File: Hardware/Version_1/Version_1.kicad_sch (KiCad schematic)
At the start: 90 parts, among them IC1 W25R256JVEIQ, IC3 TPS62A01DRLR, IC4 TPS62A01DRLR, IC5 TPS62A01DRLR, IC6 LIFCL-40-7BG256C, IC7 IS46TR16128D-125KBLA2, J1 GPIO, J2 52435-2271, J3 Conn_01x05_Pin, J4 52435-2271, U1 CAT24C256

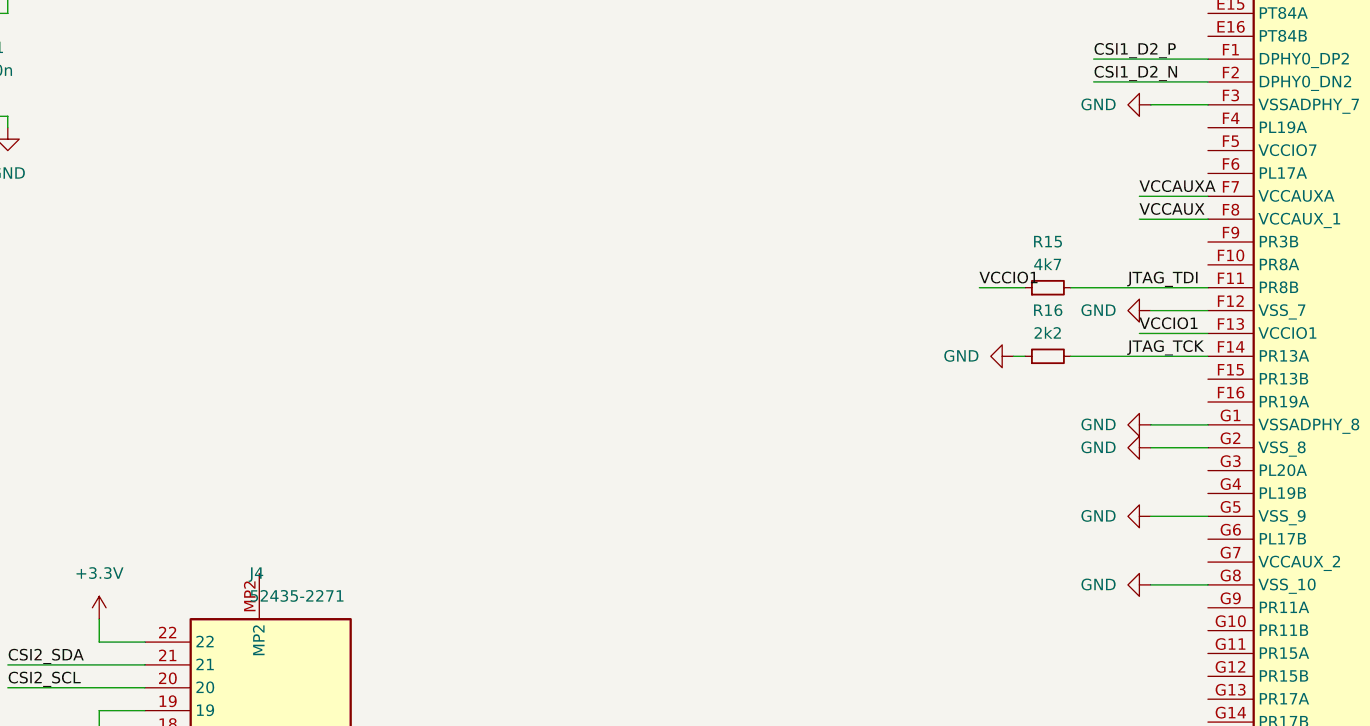
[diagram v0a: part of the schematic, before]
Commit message: added pll
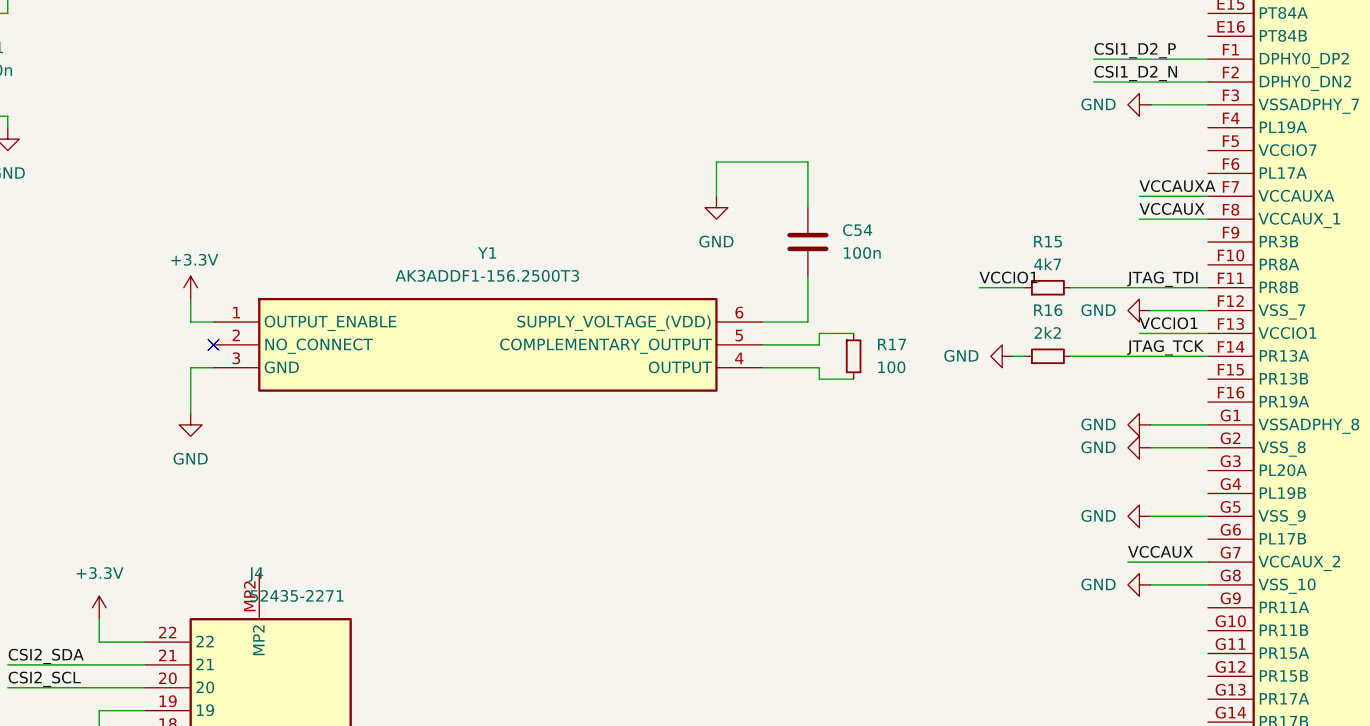
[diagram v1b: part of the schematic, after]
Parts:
- added C54: 100n, Capacitor_SMD:C_0603_1608Metric, symbol Device:C
- added R17: 100, Resistor_SMD:R_0603_1608Metric, symbol Device:R_Small
- added Y1: AK3ADDF1-156.2500T3, Component:AK3ADDF11562500T3, symbol Component:AK3ADDF1-156.2500T3
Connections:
- net +3V3: now also Y1.1 (OUTPUT_ENABLE)
- net GND: now also C54.1, Y1.3 (GND)
- net VCCAUX: now also IC6.G7 (VCCAUX_2)
- new net: C54.2, Y1.6 (SUPPLY_VOLTAGE_(VDD))
- new net: R17.1, Y1.5 (COMPLEMENTARY_OUTPUT)
- new net: R17.2, Y1.4 (OUTPUT)
- no-connect marks 20 -> 21

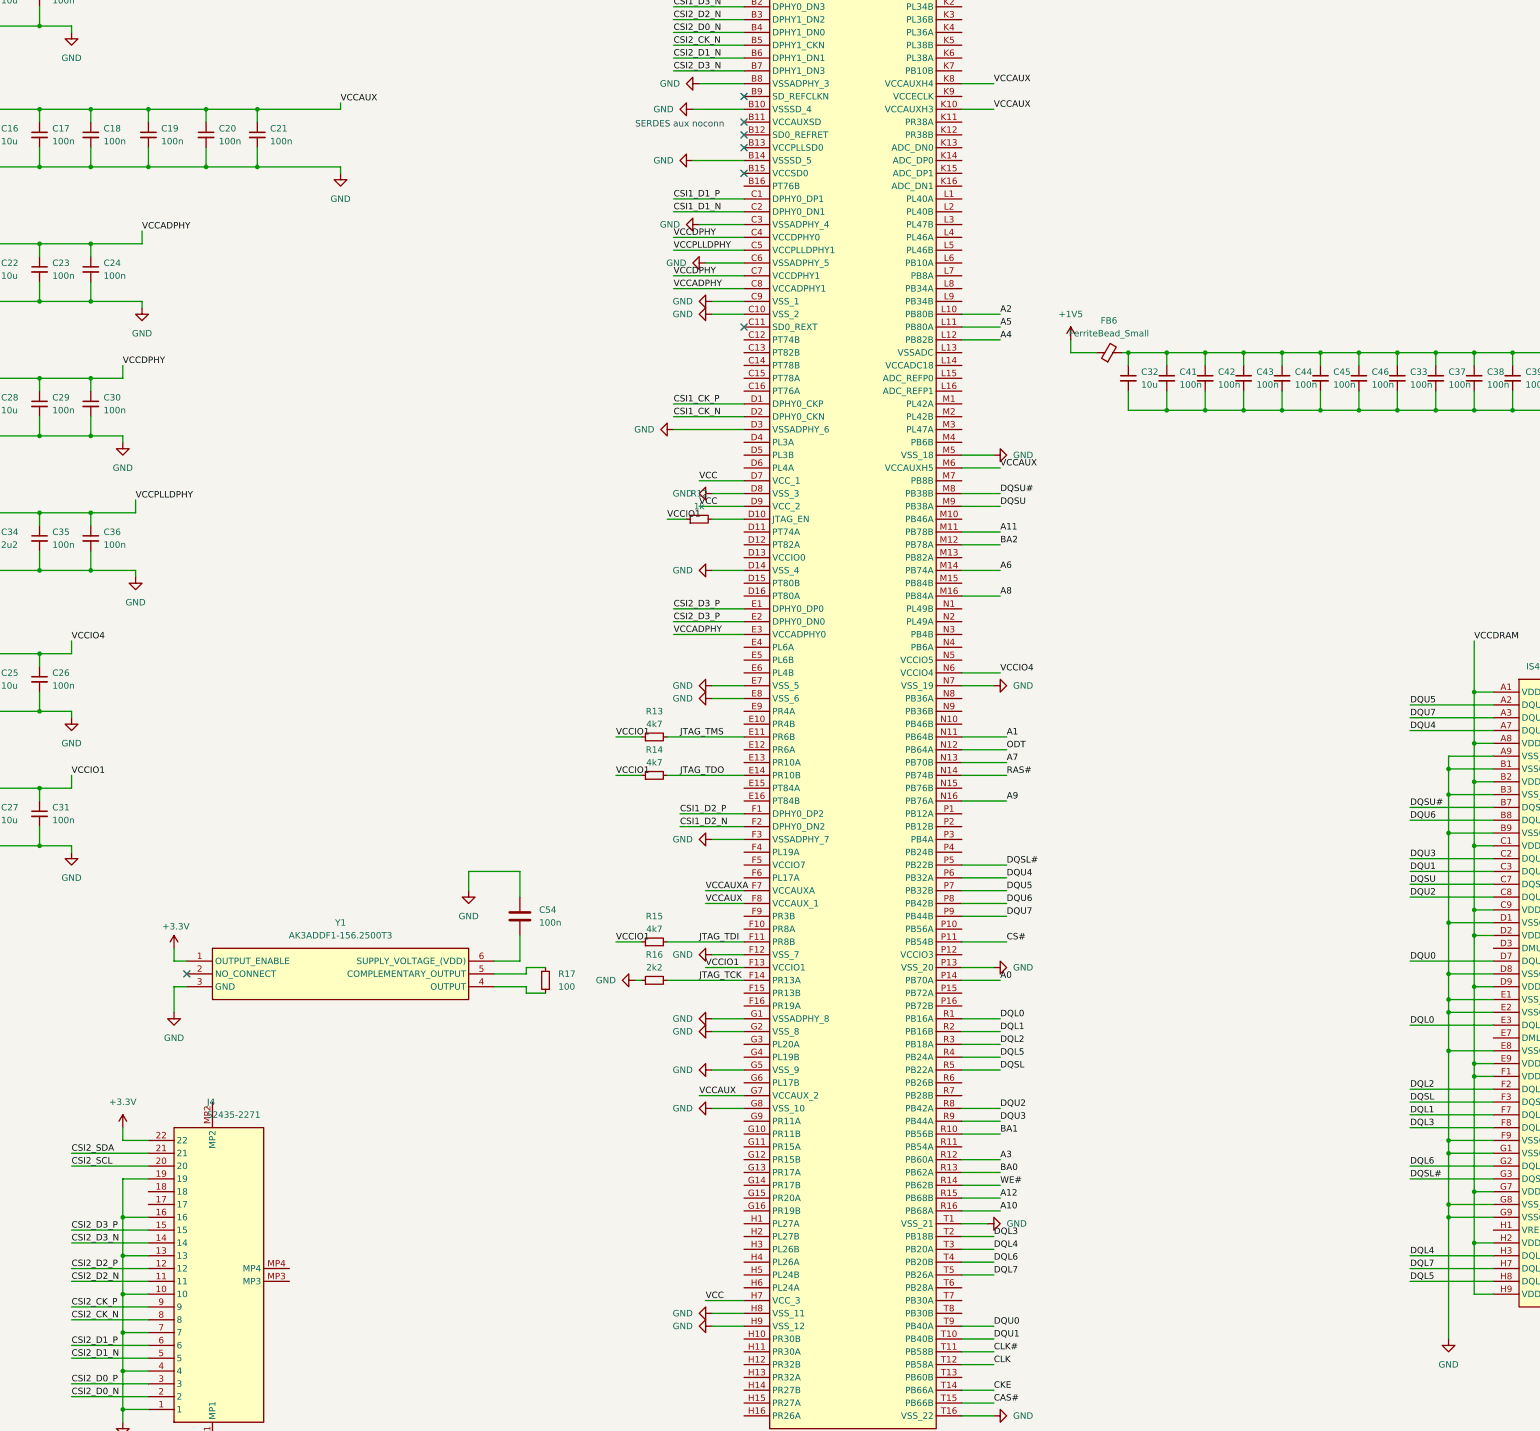
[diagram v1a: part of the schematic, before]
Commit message: Done routing for first DQS group
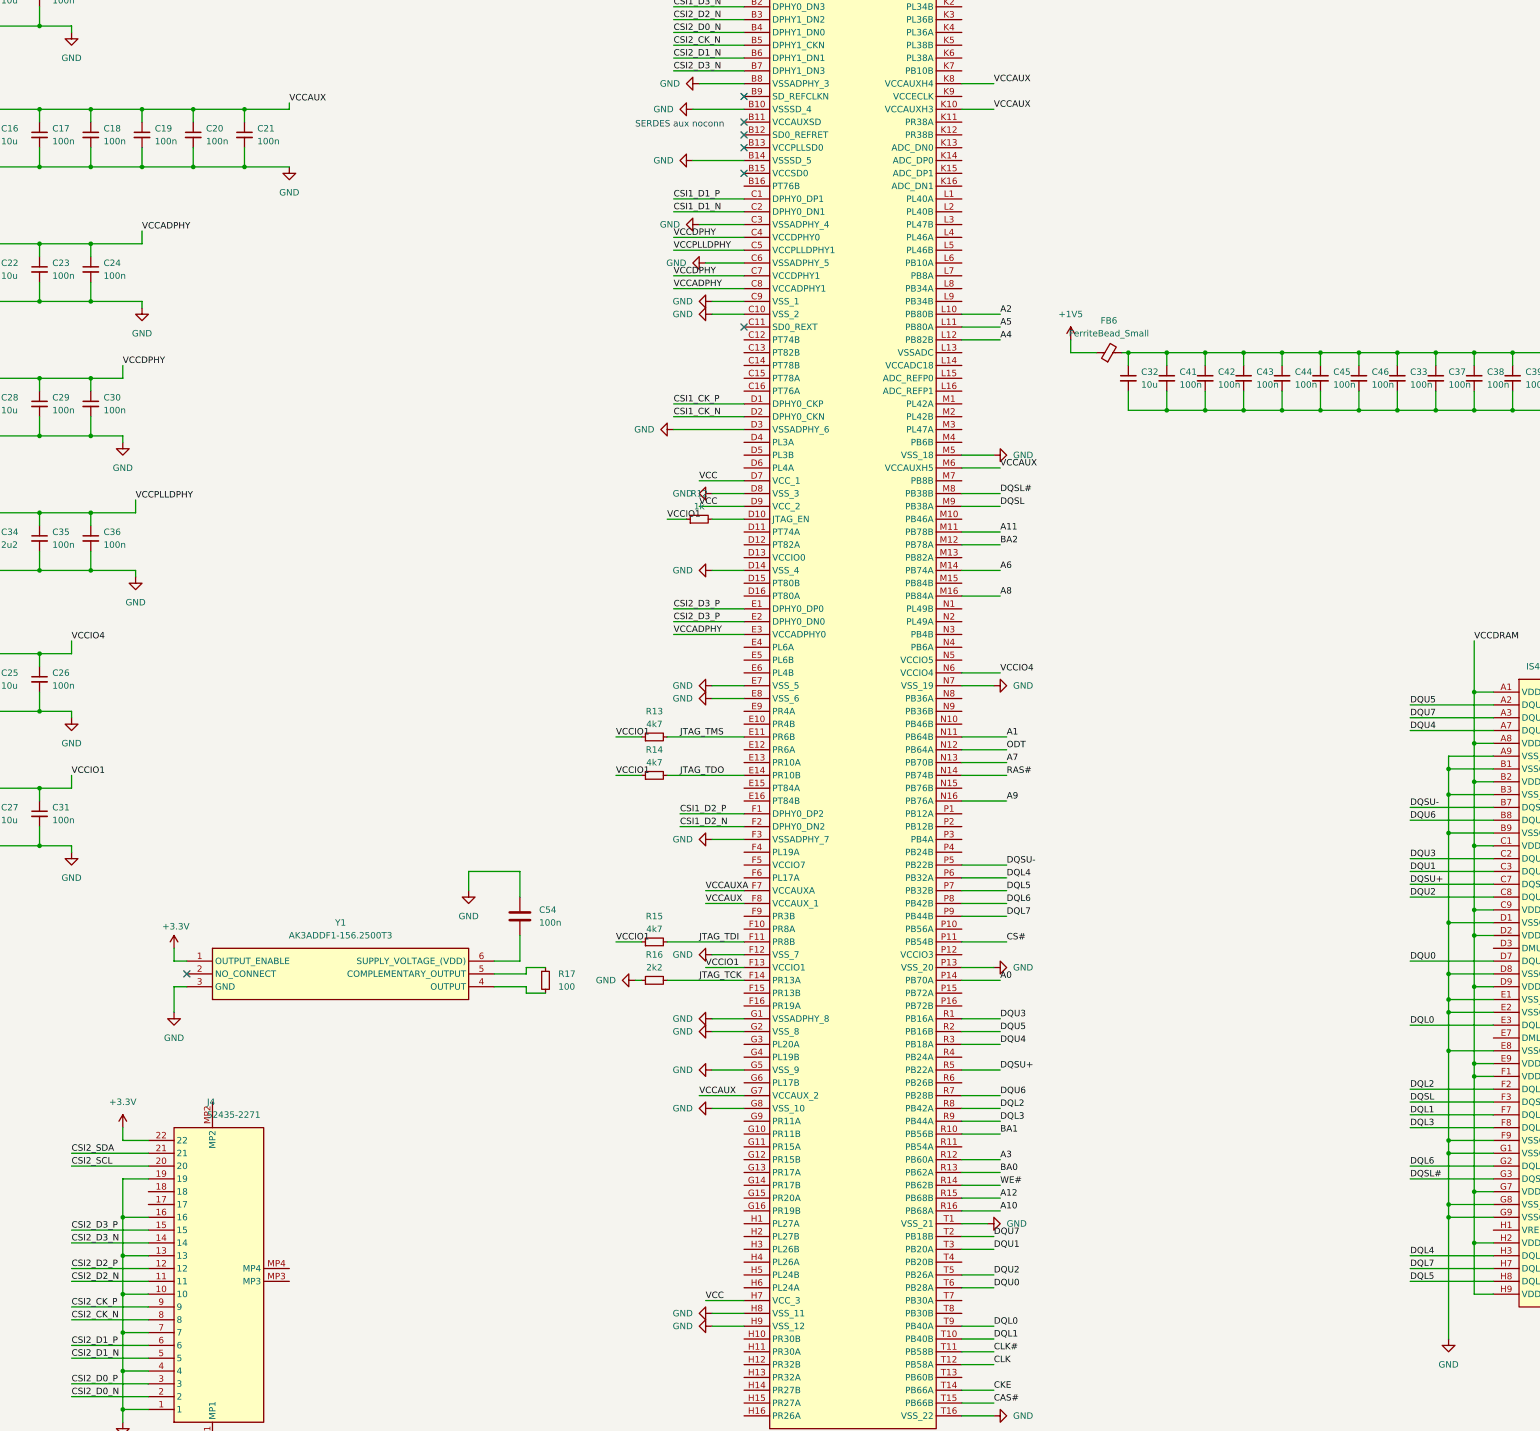
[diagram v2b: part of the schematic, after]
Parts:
- C14, C22, C25, C27, C28, C32, C34, C54, C9: footprint Capacitor_SMD:C_0603_1608Metric -> Capacitor_SMD:C_0402_1005Metric
- R13, R14, R15, R16: footprint Resistor_SMD:R_0603_1608Metric -> Resistor_SMD:R_0402_1005Metric
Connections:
- net DQL0: now also IC6.T9 (PB40A); no longer IC6.R1 (PB16A)
- net DQL1: now also IC6.T10 (PB40B); no longer IC6.R2 (PB16B)
- net DQL2: now also IC6.R8 (PB42A); no longer IC6.R3 (PB18A)
- net DQL3: now also IC6.R9 (PB44A); no longer IC6.T2 (PB18B)
- net DQL4: now also IC6.P6 (PB32A); no longer IC6.T3 (PB20A)
- net DQL5: now also IC6.P7 (PB32B); no longer IC6.R4 (PB24A)
- net DQL6: now also IC6.P8 (PB42B); no longer IC6.T4 (PB20B)
- net DQL7: now also IC6.P9 (PB44B); no longer IC6.T5 (PB26A)
- net DQSL: now also IC6.M9 (PB38A); no longer IC6.R5 (PB22A)
- net DQSL#: now also IC6.M8 (PB38B); no longer IC6.P5 (PB22B)
- net DQU0: now also IC6.T6 (PB28A); no longer IC6.T9 (PB40A)
- net DQU1: now also IC6.T3 (PB20A); no longer IC6.T10 (PB40B)
- net DQU2: now also IC6.T5 (PB26A); no longer IC6.R8 (PB42A)
- net DQU3: now also IC6.R1 (PB16A); no longer IC6.R9 (PB44A)
- net DQU4: now also IC6.R3 (PB18A); no longer IC6.P6 (PB32A)
- net DQU5: now also IC6.R2 (PB16B); no longer IC6.P7 (PB32B)
- net DQU6: now also IC6.R7 (PB28B); no longer IC6.P8 (PB42B)
- net DQU7: now also IC6.T2 (PB18B); no longer IC6.P9 (PB44B)
- net DQSU renamed DQSU+
- net DQSU+: now also IC6.R5 (PB22A); no longer IC6.M9 (PB38A)
- net DQSU# renamed DQSU-
- net DQSU-: now also IC6.P5 (PB22B); no longer IC6.M8 (PB38B)
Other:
- moved on the sheet: C19, C20, C21

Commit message: DRAM DQ groups
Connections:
- net DQL1: now also IC6.P6 (PB32A)
- net DQL3: now also IC6.P7 (PB32B)
- net DQL4: no longer IC6.P6 (PB32A)
- net DQL5: no longer IC6.P7 (PB32B)
- net DQSL renamed DQSL_P
- net DQSL# renamed DQSL_N
- net DQSU+ renamed DQSU_P
- net DQSU- renamed DQSU_N
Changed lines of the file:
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@@
     (effects (font (size 1.27 1.27)) (justify left bottom))
   )
-  (label "DQSU-" (at 487.68 252.73 0) (fields_autoplaced)
+  (label "DQSU_N" (at 487.68 252.73 0) (fields_autoplaced)
     (effects (font (size 1.27 1.27)) (justify left bottom))
   )
@@
     (effects (font (size 1.27 1.27)) (justify left bottom))
   )
-  (label "DQSU+" (at 487.68 267.97 0) (fields_autoplaced)
+  (label "DQSU_P" (at 487.68 267.97 0) (fields_autoplaced)
     (effects (font (size 1.27 1.27)) (justify left bottom))
   )
@@
     (effects (font (size 1.27 1.27)) (justify left bottom))
   )
-  (label "DQSL" (at 487.68 311.15 0) (fields_autoplaced)
+  (label "DQSL_P" (at 487.68 311.15 0) (fields_autoplaced)
     (effects (font (size 1.27 1.27)) (justify left bottom))
   )
@@
     (effects (font (size 1.27 1.27)) (justify left bottom))
   )
-  (label "DQSU-" (at 407.67 264.16 0) (fields_autoplaced)
+  (label "DQSU_N" (at 407.67 264.16 0) (fields_autoplaced)
     (effects (font (size 1.27 1.27)) (justify left bottom))
   )
@@
     (effects (font (size 1.27 1.27)) (justify right bottom))
   )
-  (label "DQSL" (at 406.4 193.04 0) (fields_autoplaced)
+  (label "DQSL_P" (at 406.4 193.04 0) (fields_autoplaced)
     (effects (font (size 1.27 1.27)) (justify left bottom))
   )
@@
     (effects (font (size 1.27 1.27)) (justify right bottom))
   )
-  (label "DQL4" (at 407.67 266.7 0) (fields_autoplaced)
+  (label "DQL1" (at 407.67 266.7 0) (fields_autoplaced)
     (effects (font (size 1.27 1.27)) (justify left bottom))
   )
@@
     (effects (font (size 1.27 1.27)) (justify left bottom))
   )
-  (label "DQL5" (at 407.67 269.24 0) (fields_autoplaced)
+  (label "DQL3" (at 407.67 269.24 0) (fields_autoplaced)
     (effects (font (size 1.27 1.27)) (justify left bottom))
   )
@@
     (effects (font (size 1.27 1.27)) (justify left bottom))
   )
-  (label "DQSU+" (at 406.4 304.8 0) (fields_autoplaced)
+  (label "DQSU_P" (at 406.4 304.8 0) (fields_autoplaced)
     (effects (font (size 1.27 1.27)) (justify left bottom))
   )
@@
     (effects (font (size 1.27 1.27)) (justify left bottom))
   )
-  (label "DQSL#" (at 406.4 190.5 0) (fields_autoplaced)
+  (label "DQSL_N" (at 406.4 190.5 0) (fields_autoplaced)
     (effects (font (size 1.27 1.27)) (justify left bottom))
   )
@@
     (effects (font (size 1.27 1.27)) (justify left bottom))
   )
-  (label "DQSL#" (at 487.68 326.39 0) (fields_autoplaced)
-    (effects (font (size 1.27 1.27)) (justify left bottom))
-  )
+  (label "DQSL_N" (at 487.68 326.39 0) (fields_autoplaced)
+    (effects (font (size 1.27 1.27)) (justify left bottom))
+  )
